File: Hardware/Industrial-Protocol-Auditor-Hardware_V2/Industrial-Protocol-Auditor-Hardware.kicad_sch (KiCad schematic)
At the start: 92 parts, among them J1 Jack-DC, J2 USB_C_Receptacle, J3 RS_Port, J4 Batt_Port, J5 CAN_Port, J6 Conn_01x08, J7 E07-M1101D-SMA, M1 Motor_DC, Q1 AO3400A, SW1 UP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

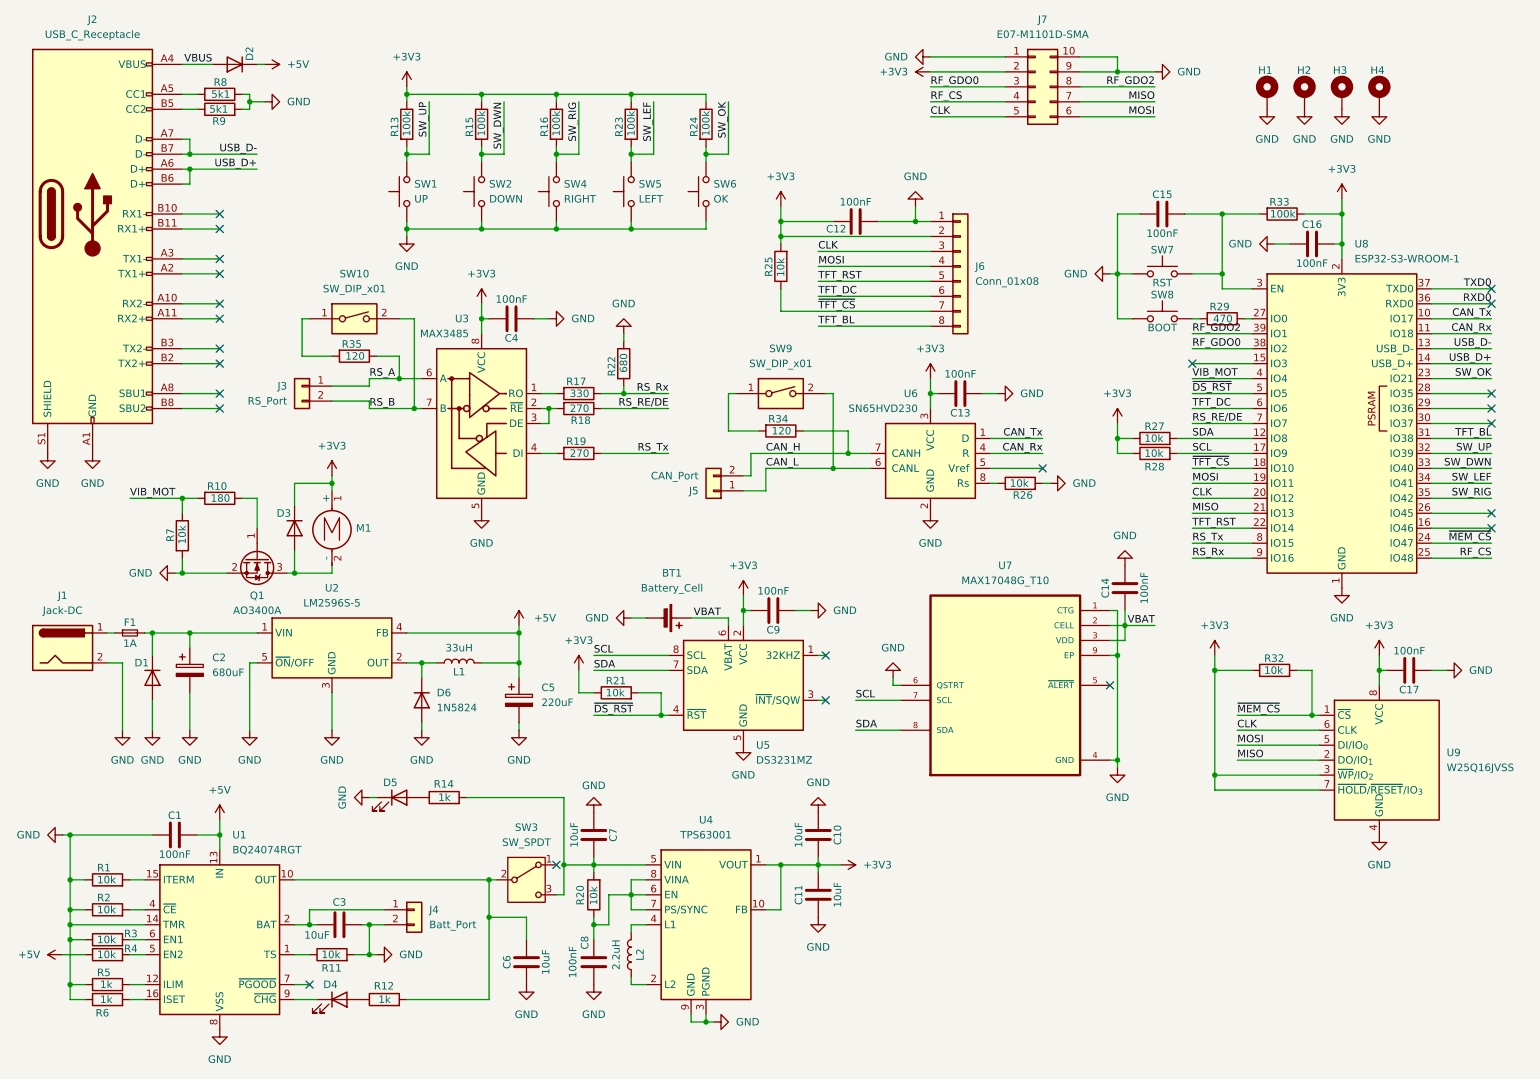
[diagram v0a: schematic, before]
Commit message: Created the ESP-IDF project wioth Vs Code extension to try ESP32-S3 microcontroller in the custom PCB for the device.
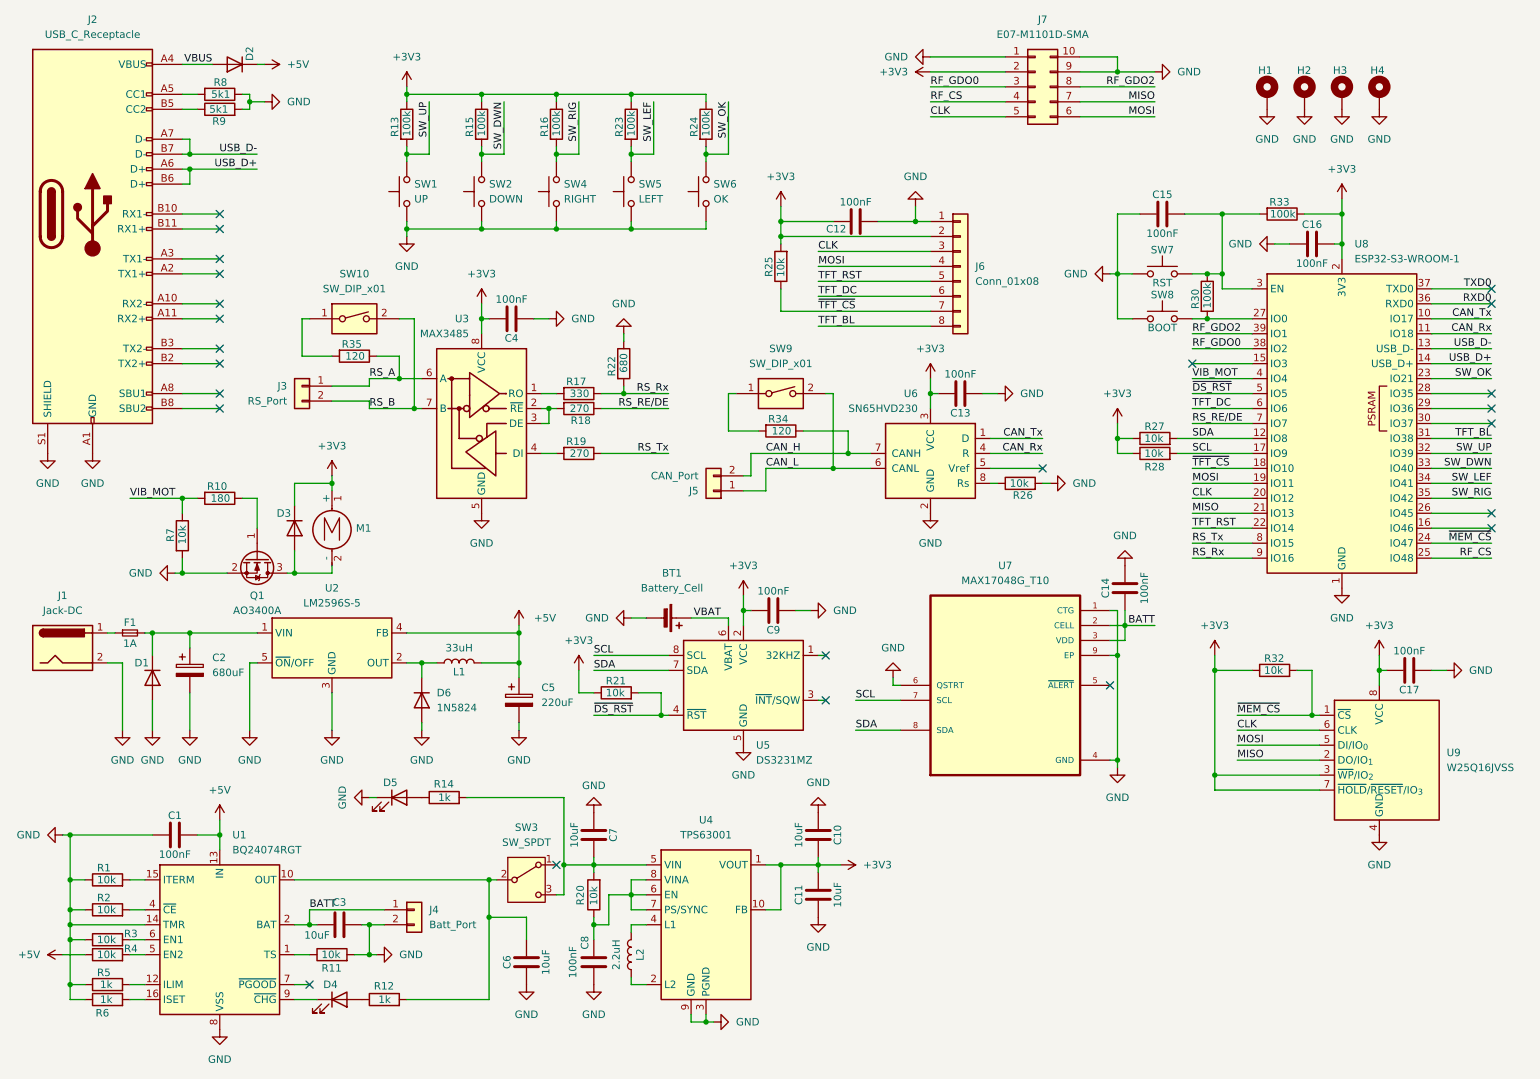
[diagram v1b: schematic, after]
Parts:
- removed R29: 470, Resistor_SMD:R_0603_1608Metric, symbol Device:R
- added R30: 100k, Resistor_SMD:R_0603_1608Metric, symbol Device:R
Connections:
- net VBAT: no longer C14.1, U7.2 (CELL), U7.3 (VDD)
- net BATT: now reaches C3.1, J4.1 (Pin_1), U1.2 (BAT), U1.3 (BAT)
- net BATT: now also C14.1, U7.2 (CELL), U7.3 (VDD)
- net at U8.27 (IO0): now also SW8.2, R30.2
- net at C15.2, R33.2, SW7.2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: now also R30.1
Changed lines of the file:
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@@
 	)
 	(junction
+		(at 224.79 63.5)
+		(diameter 0)
+		(color 0 0 0 0)
+	)
+	(junction
 		(at 152.4 57.15)
 		(diameter 0)
@@
 	)
 	(junction
+		(at 224.79 71.12)
+		(diameter 0)
+		(color 0 0 0 0)
+	)
+	(junction
 		(at 101.6 33.02)
 		(diameter 0)
@@
 	(wire
 		(pts
-			(xy 222.25 71.12) (xy 223.52 71.12)
+			(xy 222.25 71.12) (xy 224.79 71.12)
 		)
 		(stroke
@@
 	(wire
 		(pts
-			(xy 231.14 71.12) (xy 232.41 71.12)
-		)
-		(stroke
-			(width 0)
-			(type default)
-		)
-	)
-	(wire
-		(pts
 			(xy 85.09 173.99) (xy 82.55 173.99)
 		)
@@
 	(wire
 		(pts
-			(xy 222.25 63.5) (xy 227.33 63.5)
+			(xy 222.25 63.5) (xy 224.79 63.5)
 		)
 		(stroke
@@
 	(wire
 		(pts
+			(xy 224.79 63.5) (xy 227.33 63.5)
+		)
+		(stroke
+			(width 0)
+			(type default)
+		)
+	)
+	(wire
+		(pts
 			(xy 50.8 101.6) (xy 50.8 104.14)
 		)
@@
 	(wire
 		(pts
+			(xy 224.79 71.12) (xy 232.41 71.12)
+		)
+		(stroke
+			(width 0)
+			(type default)
+		)
+	)
+	(wire
+		(pts
 			(xy 226.06 151.13) (xy 243.84 151.13)
 		)
@@
 		)
 	)
+	(label "BATT"
+		(at 72.39 171.45 0)
+		(effects
+			(font
+				(size 1.27 1.27)
+			)
+			(justify left bottom)
+		)
+	)
 	(label "MISO"
 		(at 222.25 104.14 0)
@@
 		)
 	)
-	(label "VBAT"
-		(at 215.9 123.19 180)
-		(effects
-			(font
-				(size 1.27 1.27)
-			)
-			(justify right bottom)
-		)
-	)
 	(label "TXD0"
 		(at 273.05 66.04 180)
@@
 		)
 	)
+	(label "BATT"
+		(at 215.9 123.19 180)
+		(effects
+			(font
+				(size 1.27 1.27)
+			)
+			(justify right bottom)
+		)
+	)
 	(label "RS_Rx"
 		(at 133.35 83.82 180)
@@
 	)
 	(symbol
-		(lib_id "Device:C")
-		(at 158.75 158.75 0)
+		(lib_id "Device:R")
+		(at 224.79 67.31 0)
 		(unit 1)
 		(exclude_from_sim no)
@@
 		(on_board yes)
 		(dnp no)
-		(property "Reference" "C10"
-			(at 162.052 158.75 90)
+		(property "Reference" "R30"
+			(at 222.758 66.04 90)
 			(effects
 				(font
 					(size 1.27 1.27)
 				)
+				(justify right)
 			)
 		)
-		(property "Value" "10uF"
-			(at 155.448 158.75 90)
+		(property "Value" "100k"
+			(at 224.79 65.024 90)
 			(effects
 				(font
 					(size 1.27 1.27)
 				)
+				(justify right)
 			)
 		)
-		(property "Footprint" "Capacitor_SMD:C_0603_1608Metric"
-			(at 159.7152 162.56 0)
+		(property "Footprint" "Resistor_SMD:R_0603_1608Metric"
+			(at 223.012 67.31 90)
 			(effects
 				(font
@@
 		)
 		(property "Datasheet" "~"
-			(at 158.75 158.75 0)
+			(at 224.79 67.31 0)
 			(effects
 				(font
@@
 			)
 		)
-		(property "Description" "Unpolarized capacitor"
-			(at 158.75 158.75 0)
+		(property "Description" "Resistor"
+			(at 224.79 67.31 0)
 			(effects
 				(font
@@
 			)
 		)
-		(property "LCSC Part" "C19702"
-			(at 158.75 158.75 90)
+		(property "LCSC Part" "C25803"
+			(at 224.79 67.31 90)
 			(effects
 				(font
@@
 			)
 		)
-		(property "Price" "0.0056"
-			(at 158.75 158.75 90)
+		(property "Price" "0.0010"
+			(at 224.79 67.31 90)
 			(effects
 				(font
@@
 			)
 		)
-		(pin "2"
-		)
 		(pin "1"
 		)
+		(pin "2"
+		)
 		(instances
-			(project "Industrial Protocol Auditor Board"
+			(project "Industrial-Protocol-Auditor-Hardware"
 				(path "/056f334c-866c-4662-b79d-4132ffa91d09"
-					(reference "C10")
+					(reference "R30")
 					(unit 1)
 				)
@@
 	)
 	(symbol
-		(lib_id "power:GND")
-		(at 49.53 114.3 270)
+		(lib_id "Device:C")
+		(at 158.75 158.75 0)
 		(unit 1)
 		(exclude_from_sim no)
@@
 		(on_board yes)
 		(dnp no)
-		(fields_autoplaced yes)
-		(property "Reference" "#PWR07"
-			(at 43.18 114.3 0)
+		(property "Reference" "C10"
+			(at 162.052 158.75 90)
+			(effects
+				(font
+					(size 1.27 1.27)
+				)
+			)
+		)
+		(property "Value" "10uF"
+			(at 155.448 158.75 90)
+			(effects
+				(font
+					(size 1.27 1.27)
+				)
+			)
+		)
+		(property "Footprint" "Capacitor_SMD:C_0603_1608Metric"
+			(at 159.7152 162.56 0)
 			(effects
 				(font
@@
 			)
 		)
-		(property "Value" "GND"
-			(at 45.72 114.2999 90)
+		(property "Datasheet" "~"
+			(at 158.75 158.75 0)
 			(effects
 				(font
 					(size 1.27 1.27)
 				)
-				(justify right)
+				(hide yes)
 			)
 		)
-		(property "Footprint" ""
-			(at 49.53 114.3 0)
+		(property "Description" "Unpolarized capacitor"
+			(at 158.75 158.75 0)
 			(effects
 				(font
@@
 			)
 		)
-		(property "Datasheet" ""
-			(at 49.53 114.3 0)
+		(property "LCSC Part" "C19702"
+			(at 158.75 158.75 90)
 			(effects
 				(font
@@
 			)
 		)
-		(property "Description" "Power symbol creates a global label with name \"GND\" , ground"
-			(at 49.53 114.3 0)
+		(property "Price" "0.0056"
+			(at 158.75 158.75 90)
 			(effects
 				(font
@@
 			)
 		)
+		(pin "2"
+		)
 		(pin "1"
 		)
@@
 			(project "Industrial Protocol Auditor Board"
 				(path "/056f334c-866c-4662-b79d-4132ffa91d09"
-					(reference "#PWR07")
+					(reference "C10")
 					(unit 1)
 				)
@@
 	)
 	(symbol
-		(lib_id "power:+3V3")
-		(at 247.65 50.8 0)
+		(lib_id "power:GND")
+		(at 49.53 114.3 270)
 		(unit 1)
 		(exclude_from_sim no)
@@
 		(dnp no)
 		(fields_autoplaced yes)
-		(property "Reference" "#PWR058"
-			(at 247.65 54.61 0)
+		(property "Reference" "#PWR07"
+			(at 43.18 114.3 0)
 			(effects
 				(font
@@
 			)
 		)
-		(property "Value" "+3V3"
-			(at 247.65 45.72 0)
+		(property "Value" "GND"
+			(at 45.72 114.2999 90)
 			(effects
 				(font
 					(size 1.27 1.27)
 				)
+				(justify right)
 			)
 		)
 		(property "Footprint" ""
-			(at 247.65 50.8 0)
+			(at 49.53 114.3 0)
 			(effects
 				(font
@@
 		)
 		(property "Datasheet" ""
-			(at 247.65 50.8 0)
+			(at 49.53 114.3 0)
 			(effects
 				(font
@@
 			)
 		)
-		(property "Description" "Power symbol creates a global label with name \"+3V3\""
-			(at 247.65 50.8 0)
+		(property "Description" "Power symbol creates a global label with name \"GND\" , ground"
+			(at 49.53 114.3 0)
 			(effects
 				(font
@@
 		)
 		(instances
-			(project ""
+			(project "Industrial Protocol Auditor Board"
 				(path "/056f334c-866c-4662-b79d-4132ffa91d09"
-					(reference "#PWR058")
+					(reference "#PWR07")
 					(unit 1)
 				)
@@
 	)
 	(symbol
-		(lib_id "Device:R")
-		(at 227.33 71.12 270)
+		(lib_id "power:+3V3")
+		(at 247.65 50.8 0)
 		(unit 1)
 		(exclude_from_sim no)
@@
 		(on_board yes)
 		(dnp no)
-		(property "Reference" "R29"
-			(at 228.6 69.088 90)
-			(effects
-				(font
-					(size 1.27 1.27)
-				)
-				(justify right)
-			)
-		)
-		(property "Value" "470"
-			(at 229.108 71.12 90)
-			(effects
-				(font
-					(size 1.27 1.27)
-				)
-				(justify right)
-			)
-		)
-		(property "Footprint" "Resistor_SMD:R_0603_1608Metric"
-			(at 227.33 69.342 90)
+		(fields_autoplaced yes)
+		(property "Reference" "#PWR058"
+			(at 247.65 54.61 0)
 			(effects
 				(font
@@
 			)
 		)
-		(property "Datasheet" "~"
-			(at 227.33 71.12 0)
+		(property "Value" "+3V3"
+			(at 247.65 45.72 0)
 			(effects
 				(font
 					(size 1.27 1.27)
 				)
-				(hide yes)
 			)
 		)
-		(property "Description" "Resistor"
-			(at 227.33 71.12 0)
+		(property "Footprint" ""
+			(at 247.65 50.8 0)
 			(effects
 				(font
@@
 			)
 		)
-		(property "LCSC Part" "C23179"
-			(at 227.33 71.12 90)
+		(property "Datasheet" ""
+			(at 247.65 50.8 0)
 			(effects
 				(font
@@
 			)
 		)
-		(property "Price" "0.0011"
-			(at 227.33 71.12 90)
+		(property "Description" "Power symbol creates a global label with name \"+3V3\""
+			(at 247.65 50.8 0)
 			(effects
 				(font
@@
 		(pin "1"
 		)
-		(pin "2"
-		)
 		(instances
-			(project "Industrial Protocol Auditor Board"
+			(project ""
 				(path "/056f334c-866c-4662-b79d-4132ffa91d09"
-					(reference "R29")
+					(reference "#PWR058")
 					(unit 1)
 				)
